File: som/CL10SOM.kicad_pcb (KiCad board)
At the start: 4 copper layers, 34 x 32 mm, 54 parts, among them IC1 10CL025YU256C8G, J1 Conn_01x02_Pin, U1 MT46H32M16LFBF-5 IT:C, U2 MX25L12833FM2, U6 AT93C46DN-SH-T, U7 SG3225CAN 50.0000M-TJGA6, X1 DF40C-120DS-0.4V51

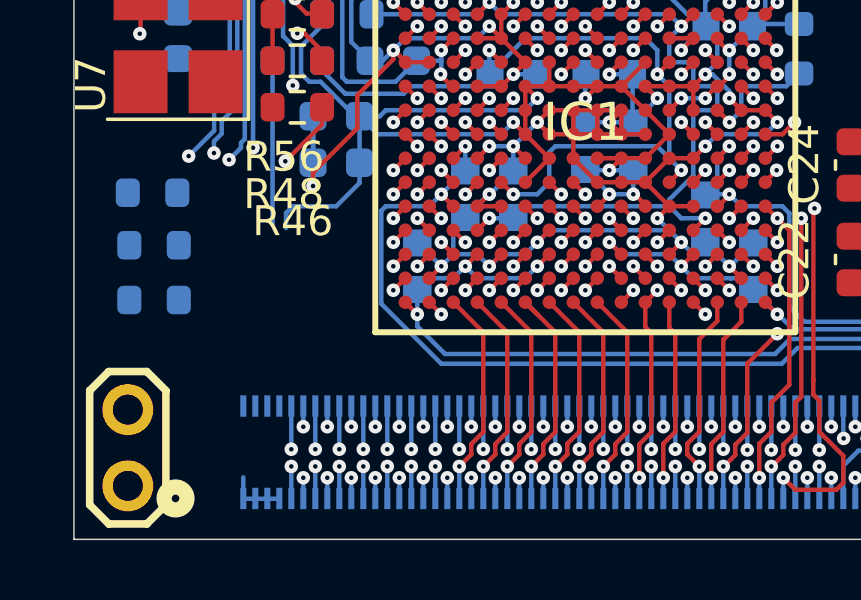
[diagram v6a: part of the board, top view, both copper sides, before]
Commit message: All I/O connected
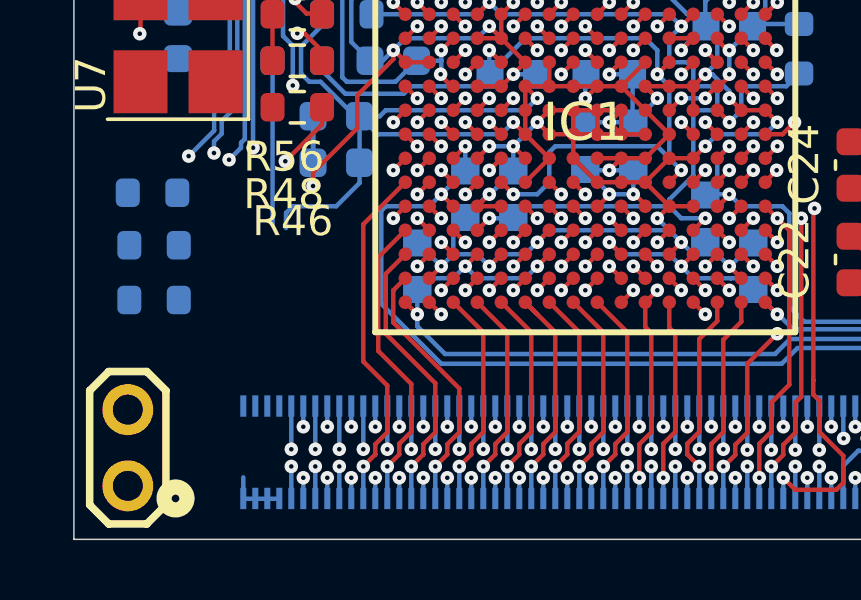
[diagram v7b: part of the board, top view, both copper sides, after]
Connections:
- X1 pad 19: unconnected-(X1-Pad19) -> /B2-IO3p
- X1 pad 20: unconnected-(X1-Pad20) -> /B2-IO2p
- X1 pad 21: unconnected-(X1-Pad21) -> /B2-IO3n
- X1 pad 22: unconnected-(X1-Pad22) -> /B2-IO2n
- X1 pad 23: unconnected-(X1-Pad23) -> /B2-IO5p
- X1 pad 24: unconnected-(X1-Pad24) -> /B2-IO1p
- X1 pad 25: unconnected-(X1-Pad25) -> /B2-IO5n
- X1 pad 26: unconnected-(X1-Pad26) -> /B2-IO1n
- X1 pad 27: unconnected-(X1-Pad27) -> /B2-IO9p
- X1 pad 28: unconnected-(X1-Pad28) -> /B2-CLK2
- X1 pad 29: unconnected-(X1-Pad29) -> /B2-IO9n
- X1 pad 30: unconnected-(X1-Pad30) -> /B2-CLK3
- X1 pad 31: unconnected-(X1-Pad31) -> /B2-IO7
- X1 pad 32: unconnected-(X1-Pad32) -> /B2-IO6
- X1 pad 33: unconnected-(X1-Pad33) -> /B2-IO8
- X1 pad 34: unconnected-(X1-Pad34) -> /B2-IO4
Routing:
- net /B2-IO4: track 4.06 -> 16.4 mm, vias 1 -> 2
- net /B2-IO1n: track 3.04 -> 13.3 mm, vias 1 -> 2
- net /B2-IO2n: track 2.52 -> 12.5 mm, vias 1 -> 2
- net /B2-IO3n: track 2.25 -> 11.8 mm
- net /B2-IO3p: track 3.43 -> 12.1 mm, vias 1 -> 2
- net /B2-CLK3: track 2.44 -> 10.2 mm, vias 1 -> 2
- net /B2-IO2p: track 3.46 -> 11.1 mm, vias 1 -> 2
- net /B2-IO5n: track 2.49 -> 10.1 mm
- net /B2-IO1p: track 4.28 -> 11.8 mm, vias 1 -> 2
- net /B2-IO5p: track 3.43 -> 10.7 mm, vias 1 -> 2
- net /B2-IO9n: track 2.44 -> 9.43 mm
- net /B2-IO7: track 5.11 -> 11.7 mm, vias 1 -> 2
- net /B2-IO8: track 2.39 -> 8.75 mm
- net /B2-IO9p: track 3.38 -> 9.22 mm, vias 1 -> 2
- net /B2-IO6: track 5.88 -> 11.0 mm, vias 1 -> 2
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
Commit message: Some cleanup
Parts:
- moved R57 6.77 mm to (92.5, 66.5), turned to 180 degrees
- moved R59 5.72 mm to (90.8, 69.6)
- moved R58 4.89 mm to (90.8, 68.1)
- moved R47 0.10 mm to (107.6, 60.0)
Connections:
- X1 pad 12: /TDI -> /TDO
- X1 pad 18: unconnected-(X1-Pad18) -> /B1-CLK1
- X1 pad 9: /TDO -> /TDI
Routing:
- net +5V: track 13.8 -> 70.0 mm
- net /TDI: track 10.5 -> 22.3 mm, vias 2 -> 3
- net /EEDO: track 4.63 -> 15.5 mm, vias 1 -> 2
- net /TMS: track 10.6 -> 20.3 mm, vias 2 -> 3
- net /DATA0: track 24.6 -> 15.0 mm, vias 3 -> 2
- net /TCK: track 10.2 -> 19.1 mm, vias 2 -> 3
- net /DCLK: track 23.5 -> 32.0 mm, vias 4 -> 2
- net GND: track 198.2 -> 206.1 mm
- net /B1-CLK1: track 13.8 -> 20.7 mm
- net /TDO: track 8.15 -> 14.6 mm
- net /FL_D2: track 32.6 -> 26.2 mm, vias 3 -> 2
- net /B2-IO4: track 16.4 -> 12.9 mm
- net (no net): track 3.23 -> 0.00 mm
- net +3V3: track 79.7 -> 82.9 mm, vias 10 -> 11
- net /FL_D3: track 33.6 -> 31.0 mm
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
